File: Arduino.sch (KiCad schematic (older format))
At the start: 0 parts

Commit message: Arduino Modules
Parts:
- added ARD?: ARDUINOPINS, symbol ARDUINOPINS
- added R? (x13): R, ~, symbol R
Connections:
- net MISO: now also R?.2
- net MOSI: now also R?.2
- net Relay+: now also R?.2
- net Relay-: now also R?.2
- net SCLK: now also R?.2
- net TACH_MEAS: now also R?.1
- new net: ARD?.11 (Digital0), R?.1
- new net: ARD?.12 (Digital1), R?.1
- new net: ARD?.19 (Digital8), R?.1
- new net: ARD?.20 (PWM0), R?.1
- new net: ARD?.21 (CS_N), R?.1
- new net: ARD?.22 (MOSI), R?.1
- new net: ARD?.23 (MISO), R?.1
- new net: ARD?.24 (SCK), R?.1
- new net: ARD?.5 (AnalogIn0), R?.2
- new net: ARD?.6 (AnalogIn1), R?.2
- new net: ARD?.7 (AnalogIn2), R?.2
- new net: ARD?.8 (AnalogIn3), R?.2
- new net ADC_CS_N: R?.2
- new net DAC_CS_N: R?.2
- new net FAN_EN_N: R?.2
- new net GND: R?.1
- new net LED_EN_PWM: R?.2
- new net V+_ADJ_MON: R?.1
- new net V-_ADJ_MON: R?.1

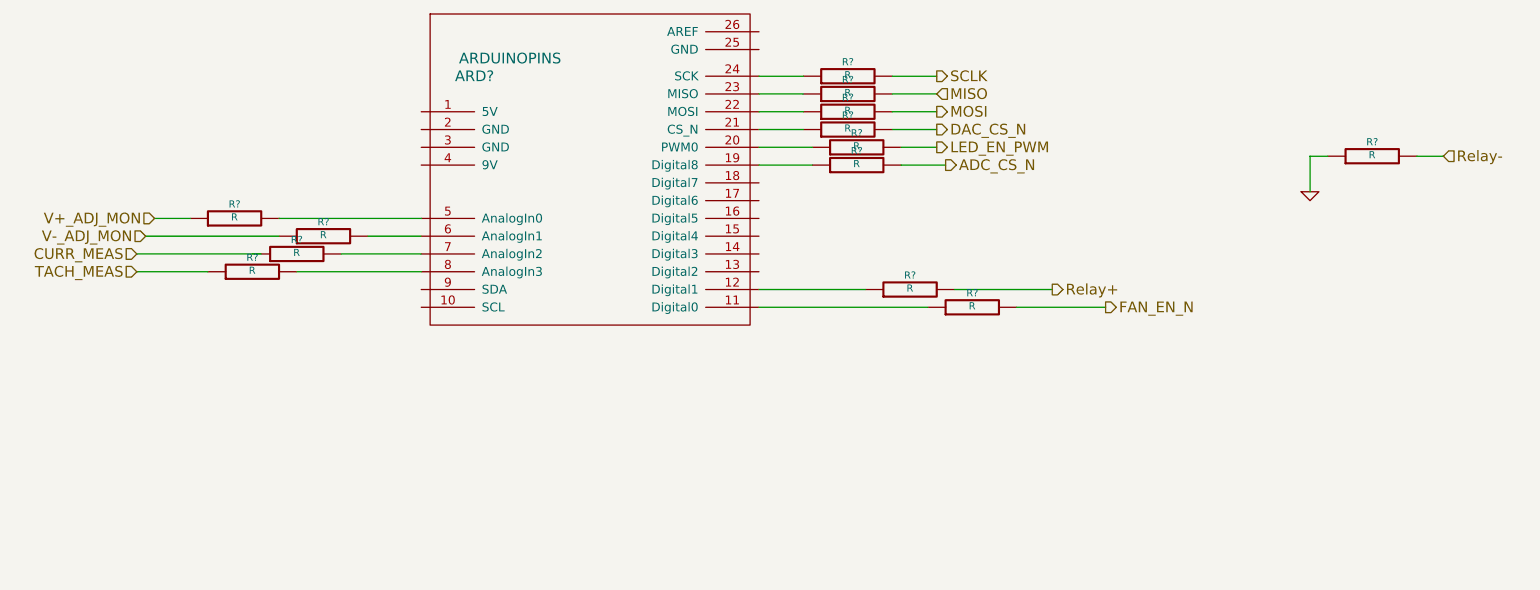
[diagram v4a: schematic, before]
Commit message: Fan/Current Module Refactoring
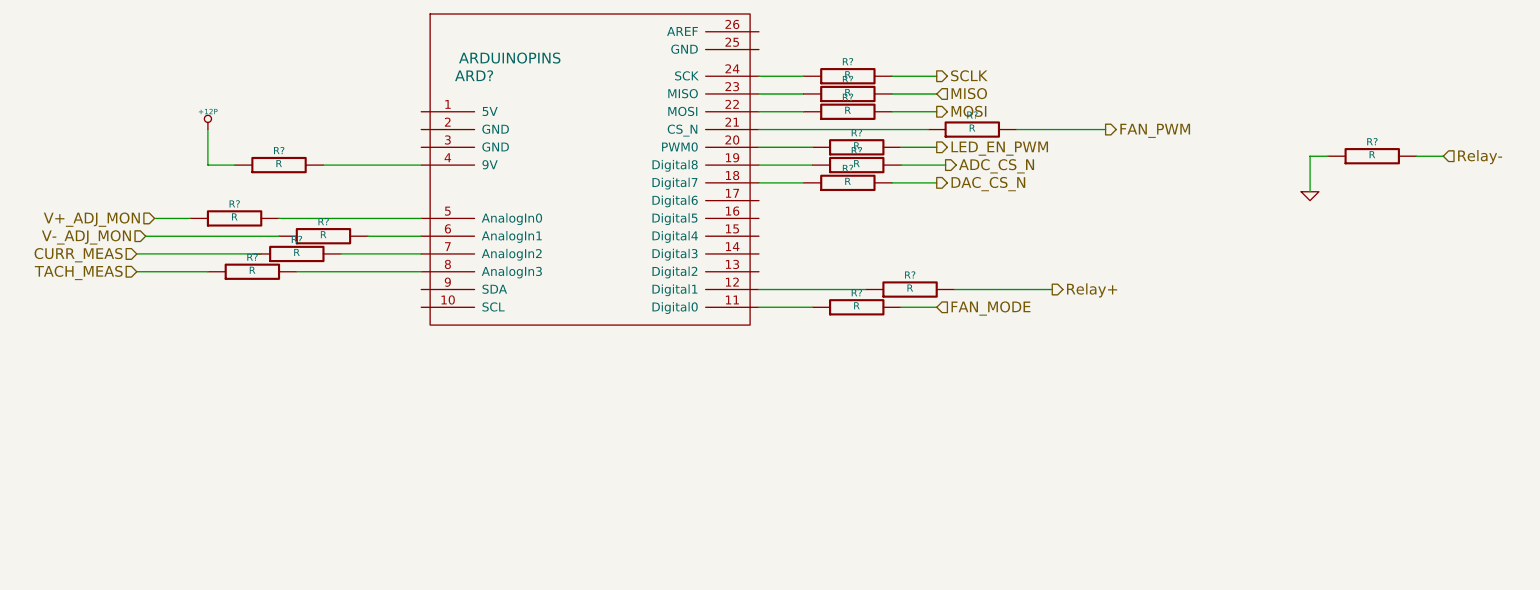
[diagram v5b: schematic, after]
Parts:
- added R? (x2): R, ~, symbol R
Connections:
- net at ARD?.11 (Digital0): now also R?.1; no longer R?.1
- net at ARD?.18 (Digital7): now also R?.1
- net at ARD?.21 (CS_N): now also R?.1; no longer R?.1
- net at ARD?.4 (9V): now also R?.2
- net FAN_EN_N renamed FAN_PWM
- new net +12P: R?.1
- new net FAN_MODE: R?.2
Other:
- moved on the sheet: R?
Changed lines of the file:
@@
 Sheet 2 9
 Title ""
-Date "24 may 2014"
+Date "25 may 2014"
 Rev ""
 Comp ""
@@
 Text HLabel 6200 2800 2    60   Output ~ 0
 SCLK
-Text HLabel 6200 3100 2    60   Output ~ 0
+Text HLabel 6200 3400 2    60   Output ~ 0
 DAC_CS_N
 Text HLabel 6200 3000 2    60   Output ~ 0
@@
 Text HLabel 6200 2900 2    60   Input ~ 0
 MISO
-Text HLabel 7150 4100 2    60   Output ~ 0
-FAN_EN_N
+Text HLabel 7150 3100 2    60   Output ~ 0
+FAN_PWM
 Text HLabel 1700 3900 0    60   Input ~ 0
 TACH_MEAS
@@
 L R R?
 U 1 1 53819741
-P 6400 4100
-F 0 "R?" V 6480 4100 40  0000 C CNN
-F 1 "R" V 6407 4101 40  0000 C CNN
-F 2 "~" V 6330 4100 30  0000 C CNN
-F 3 "~" H 6400 4100 30  0000 C CNN
-	1    6400 4100
+P 6400 3100
+F 0 "R?" V 6480 3100 40  0000 C CNN
+F 1 "R" V 6407 3101 40  0000 C CNN
+F 2 "~" V 6330 3100 30  0000 C CNN
+F 3 "~" H 6400 3100 30  0000 C CNN
+	1    6400 3100
 	0    -1   -1   0
 $EndComp
@@
 L R R?
 U 1 1 5381CBAE
-P 5700 3100
-F 0 "R?" V 5780 3100 40  0000 C CNN
-F 1 "R" V 5707 3101 40  0000 C CNN
-F 2 "~" V 5630 3100 30  0000 C CNN
-F 3 "~" H 5700 3100 30  0000 C CNN
-	1    5700 3100
+P 5700 3400
+F 0 "R?" V 5780 3400 40  0000 C CNN
+F 1 "R" V 5707 3401 40  0000 C CNN
+F 2 "~" V 5630 3400 30  0000 C CNN
+F 3 "~" H 5700 3400 30  0000 C CNN
+	1    5700 3400
 	0    -1   -1   0
 $EndComp
@@
 $EndComp
 Wire Wire Line
-	6650 4100 7150 4100
-Wire Wire Line
-	6150 4100 5200 4100
+	6650 3100 7150 3100
+Wire Wire Line
+	6150 3100 5200 3100
 Wire Wire Line
 	6300 4000 6850 4000
@@
 	5950 3000 6200 3000
 Wire Wire Line
-	5950 3100 6200 3100
+	5950 3400 6200 3400
 Wire Wire Line
 	5200 2800 5450 2800
@@
 	5200 3000 5450 3000
 Wire Wire Line
-	5200 3100 5450 3100
+	5200 3400 5450 3400
 $Comp
 L R R?
@@
 Wire Wire Line
 	6000 3300 6250 3300
+Text HLabel 6200 4100 2    60   Input ~ 0
+FAN_MODE
+$Comp
+L R R?
+U 1 1 53818284
+P 5750 4100
+F 0 "R?" V 5830 4100 40  0000 C CNN
+F 1 "R" V 5757 4101 40  0000 C CNN
+F 2 "~" V 5680 4100 30  0000 C CNN
+F 3 "~" H 5750 4100 30  0000 C CNN
+	1    5750 4100
+	0    -1   -1   0
+$EndComp
+Wire Wire Line
+	5200 4100 5500 4100
+Wire Wire Line
+	6000 4100 6200 4100
+$Comp
+L R R?
+U 1 1 53818665
+P 2500 3300
+F 0 "R?" V 2580 3300 40  0000 C CNN
+F 1 "R" V 2507 3301 40  0000 C CNN
+F 2 "~" V 2430 3300 30  0000 C CNN
+F 3 "~" H 2500 3300 30  0000 C CNN
+	1    2500 3300
+	0    -1   -1   0
+$EndComp
+Wire Wire Line
+	2750 3300 3300 3300
+$Comp
+L +12P #PWR?
+U 1 1 5381868B
+P 2100 3100
+F 0 "#PWR?" H 2100 3070 30  0001 C CNN
+F 1 "+12P" H 2100 3200 30  0000 C CNN
+F 2 "" H 2100 3100 60  0000 C CNN
+F 3 "" H 2100 3100 60  0000 C CNN
+	1    2100 3100
+	1    0    0    -1
+$EndComp
+Wire Wire Line
+	2100 3100 2100 3300
+Wire Wire Line
+	2100 3300 2250 3300
 $EndSCHEMATC
